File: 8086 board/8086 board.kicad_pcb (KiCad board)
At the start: 2 copper layers, 94 x 90 mm, 157 parts, among them J1 8086 bus, J2 USB, J3 RGB LCD, J4 UART, J5 AVR-ISP-6, SW33 RESET, SW34 MEM_BANK, U1 P8086-2, U10 29F800BA, U11 IS61C6416AL, U12 IS61C6416AL, U13 74AC573, U14 74AC573, U15 74AC573, U16 74AC573, U17 74LVC245A, U18 74LVC245A, U19 74LVC245A, U2 74HC32, U20 ATmega328P, U21 74HC595, U22 74HC595, U23 74HC595, U24 74HC165, U25 74HC165, U3 AMS1117-3.3, U4 CH340C, U5 74AC573, U6 74AC573, U7 74AC573, U8 74HC138, U9 74HC138, Y1 16MHz

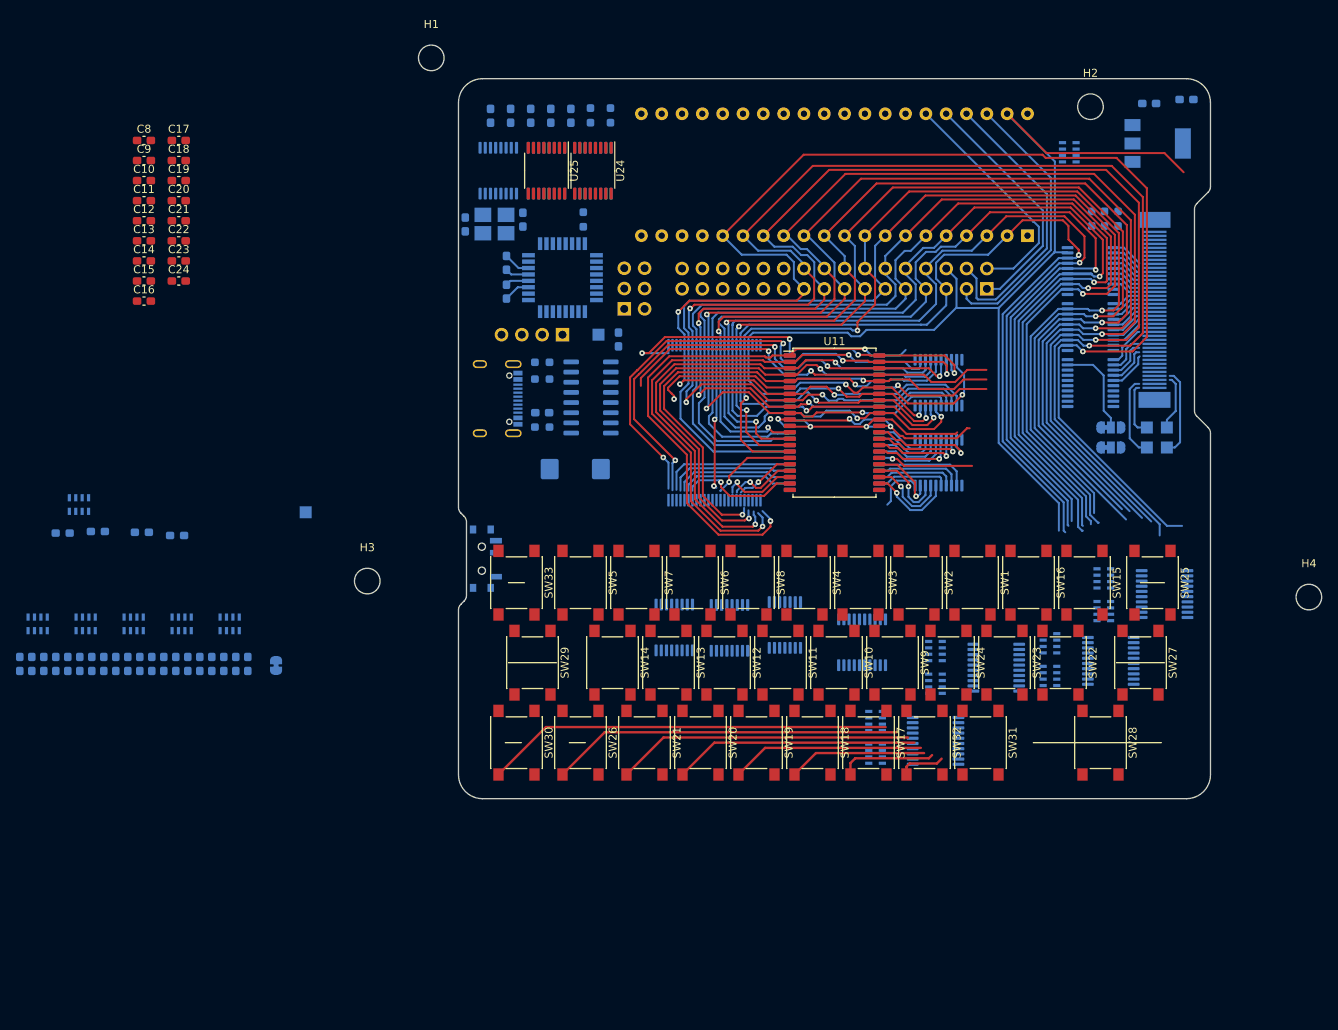
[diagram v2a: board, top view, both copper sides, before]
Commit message: PCB: layout and routing of IO, shift registers, and MCU
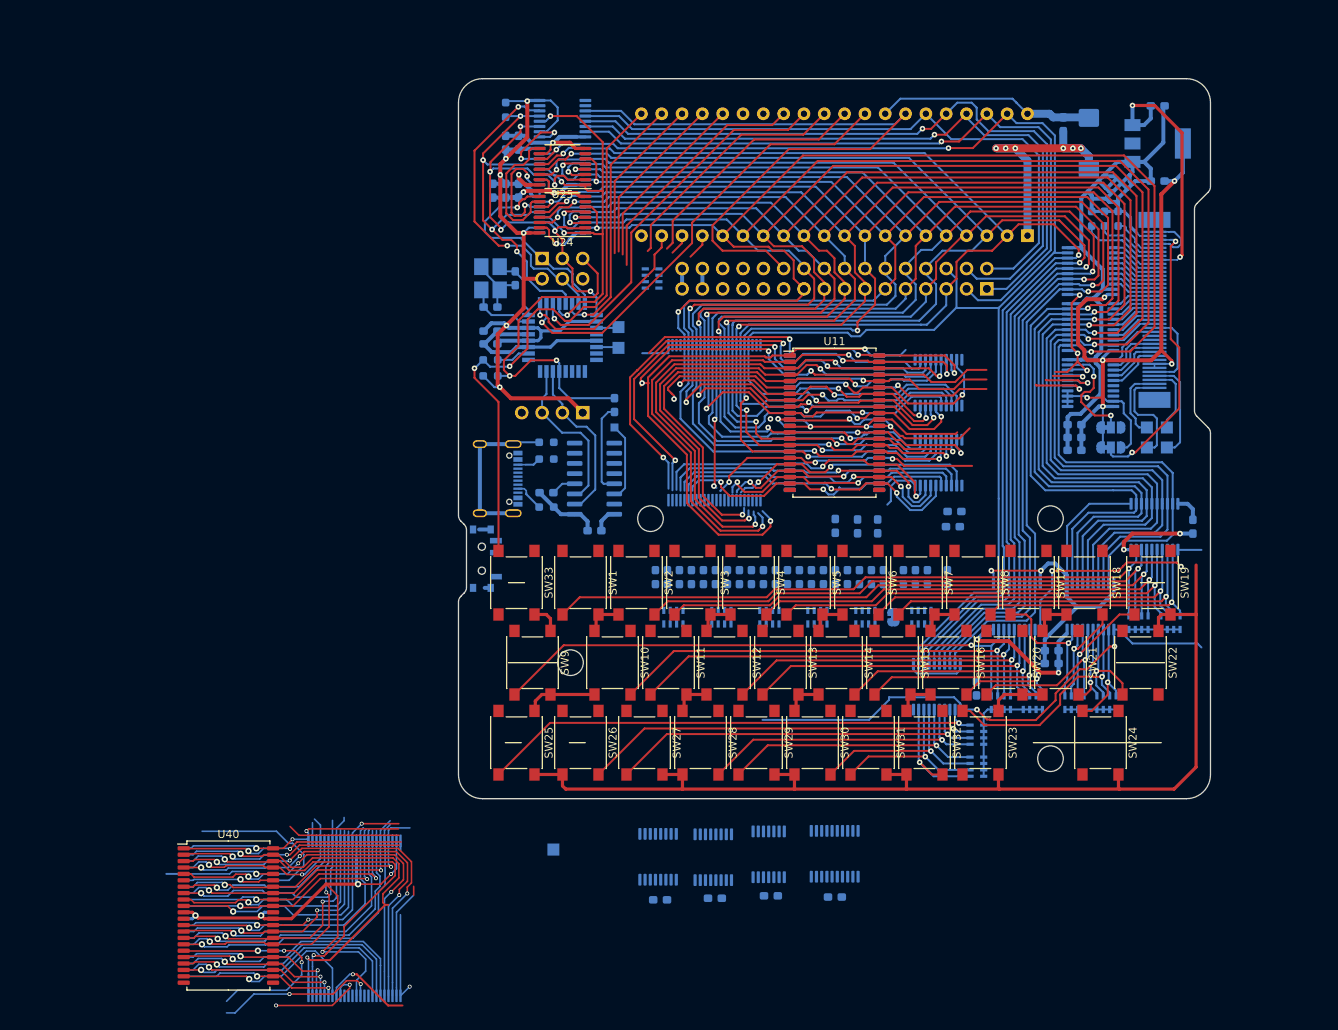
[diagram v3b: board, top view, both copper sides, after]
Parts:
- added C32: 1uF, Capacitor_SMD:C_0603_1608Metric_Pad1.08x0.95mm_HandSolder, B.Cu at (177.4, 45.1)
- added TP7: ADC6, TestPoint:TestPoint_Pad_1.5x1.5mm, B.Cu at (121.8, 70.4)
- added TP8: ADC7, TestPoint:TestPoint_Pad_1.5x1.5mm, B.Cu at (121.8, 73.0)
- added U39: 29F800BA, Package_SO:TSOP-I-48_18.4x12mm_P0.5mm, B.Cu at (88.8, 144.3)
- added U40: IS61C6416AL, Package_SO:TSOP-II-44_10.16x18.41mm_P0.8mm, F.Cu at (73.0, 144.0)
- C10, C11, C12, C13, C14, C15, C16, C17, C18, C19, C20, C21, C22, C23, C24, C8, C9: moved to B.Cu
- H1, H2, H3, H4: footprint MountingHole:MountingHole_3.2mm_M3 -> MountingHole:MountingHole_3.2mm_M3_DIN965; moved to B.Cu
- TP1: footprint TestPoint:TestPoint_Pad_1.5x1.5mm -> TestPoint:TestPoint_Pad_1.0x1.0mm
- moved C21 132.4 mm to (193.6, 95.4), turned to -90 degrees
- moved C20 123.5 mm to (175.9, 112.5)
- moved C22 120.5 mm to (175.9, 110.9)
- moved C17 117.5 mm to (178.8, 82.6), turned to 180 degrees
- moved C14 117.4 mm to (148.8, 141.7), turned to 180 degrees
- moved C18 117.2 mm to (178.8, 84.2), turned to 180 degrees
- moved C19 116.9 mm to (178.8, 85.8), turned to 180 degrees
- moved C23 113.1 mm to (166.5, 115.6), turned to -90 degrees
- moved C15 109.8 mm to (140.8, 141.5), turned to 180 degrees
- moved C11 109.0 mm to (163.6, 95.4), turned to 180 degrees
- moved D20 108.5 mm to (154.9, 101.7)
- moved C12 107.6 mm to (163.8, 93.5)
- moved RA7 106.2 mm to (159.6, 106.7)
- moved D19 105.5 mm to (153.4, 101.7)
- moved D23 105.2 mm to (157.4, 101.7), turned to 90 degrees
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- renumbered SW5 to SW1, SW14 to SW10, SW13 to SW11, SW11 to SW13, SW10 to SW14, SW9 to SW15, SW24 to SW16, SW16 to SW17, SW15 to SW18, SW25 to SW19, SW7 to SW2, SW23 to SW20, SW22 to SW21, SW27 to SW22, SW31 to SW23, SW28 to SW24, SW30 to SW25, SW21 to SW27, SW20 to SW28, SW19 to SW29, SW6 to SW3, SW18 to SW30, SW17 to SW31, SW8 to SW4, SW4 to SW5, SW3 to SW6, SW2 to SW7, SW1 to SW8, SW29 to SW9
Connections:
- net /Microcontroller/REG_OE renamed /Microcontroller/REG_~{OE}
- C17 pad 1: +5V -> +3.3V
- C18 pad 1: +5V -> +3.3V
- C19 pad 1: +5V -> +3.3V
- D1 pad 1: Net-(D1-A) -> /Memory/LA0
- D1 pad 2: /Memory/LED_CC -> Net-(D1-K)
- D10 pad 1: Net-(D10-A) -> /Memory/LA9
- D10 pad 2: /Memory/LED_CC -> Net-(D10-K)
- D11 pad 1: Net-(D11-A) -> /Memory/LA10
- D11 pad 2: /Memory/LED_CC -> Net-(D11-K)
- D12 pad 1: Net-(D12-A) -> /Memory/LA11
- D12 pad 2: /Memory/LED_CC -> Net-(D12-K)
- D13 pad 1: Net-(D13-A) -> /Memory/LA12
- D13 pad 2: /Memory/LED_CC -> Net-(D13-K)
- D14 pad 1: Net-(D14-A) -> /Memory/LA13
- D14 pad 2: /Memory/LED_CC -> Net-(D14-K)
- D15 pad 1: Net-(D15-A) -> /Memory/LA14
- D15 pad 2: /Memory/LED_CC -> Net-(D15-K)
- D16 pad 1: Net-(D16-A) -> /Memory/LA15
- D16 pad 2: /Memory/LED_CC -> Net-(D16-K)
- D17 pad 1: Net-(D17-A) -> /IO/D/~{C}
- D17 pad 2: /Memory/LED_CC -> Net-(D17-K)
- D18 pad 1: Net-(D18-A) -> /Memory/LA17
- D18 pad 2: /Memory/LED_CC -> Net-(D18-K)
- D19 pad 1: Net-(D19-A) -> /Memory/LA18
- D19 pad 2: /Memory/LED_CC -> Net-(D19-K)
- D2 pad 1: Net-(D2-A) -> /Memory/LA1
- D2 pad 2: /Memory/LED_CC -> Net-(D2-K)
- D20 pad 1: Net-(D20-A) -> /Memory/LA19
- D20 pad 2: /Memory/LED_CC -> Net-(D20-K)
- D3 pad 1: Net-(D3-A) -> /Memory/LA2
- D3 pad 2: /Memory/LED_CC -> Net-(D3-K)
- D4 pad 1: Net-(D4-A) -> /Memory/LA3
- D4 pad 2: /Memory/LED_CC -> Net-(D4-K)
- D5 pad 1: Net-(D5-A) -> /Memory/LA4
- D5 pad 2: /Memory/LED_CC -> Net-(D5-K)
- D6 pad 1: Net-(D6-A) -> /Memory/LA5
- D6 pad 2: /Memory/LED_CC -> Net-(D6-K)
- D7 pad 1: Net-(D7-A) -> /Memory/LA6
- D7 pad 2: /Memory/LED_CC -> Net-(D7-K)
- D8 pad 1: Net-(D8-A) -> /Memory/LA7
- D8 pad 2: /Memory/LED_CC -> Net-(D8-K)
- D9 pad 1: Net-(D9-A) -> /Memory/LA8
- D9 pad 2: /Memory/LED_CC -> Net-(D9-K)
- RA1 pad 1: +5V -> ~{RD}
- RA1 pad 2: +5V -> ~{WR}
- RA1 pad 3: +5V -> READY
- RA1 pad 4: GND -> RESET
- RA1 pad 5: RESET -> GND
- RA1 pad 6: ~{RD} -> +5V
- RA1 pad 7: ~{WR} -> +5V
- RA1 pad 8: READY -> +5V
- RA10 pad 1: /IO/I8 -> /IO/I9
- RA10 pad 2: /IO/I9 -> /IO/I10
- RA10 pad 3: /IO/I10 -> /IO/I11
- RA10 pad 4: /IO/I11 -> /IO/I12
- RA11 pad 1: /IO/I12 -> /IO/I13
- RA11 pad 2: /IO/I13 -> /IO/I14
- RA11 pad 3: /IO/I14 -> /IO/I15
- RA11 pad 4: /IO/I15 -> /IO/I16
- RA12 pad 1: /IO/I16 -> /IO/I17
- RA12 pad 2: /IO/I17 -> /IO/I18
- RA12 pad 3: /IO/I18 -> /IO/I19
- RA12 pad 4: /IO/I19 -> /IO/I20
- RA13 pad 1: /IO/I20 -> /IO/I21
- RA13 pad 2: /IO/I21 -> /IO/I22
- RA13 pad 3: /IO/I22 -> /IO/I23
- RA13 pad 4: /IO/I23 -> /IO/I24
- RA14 pad 1: /IO/I24 -> /IO/I28
- RA14 pad 2: /IO/I25 -> /IO/I27
- RA14 pad 4: /IO/I27 -> /IO/I25
- RA15 pad 1: /IO/I28 -> /IO/I32
- RA15 pad 2: /IO/I29 -> /IO/I31
- RA15 pad 4: /IO/I31 -> /IO/I29
- RA2 pad 1: Net-(D4-A) -> /Memory/LED_CC
- RA2 pad 2: Net-(D3-A) -> /Memory/LED_CC
- RA2 pad 3: Net-(D2-A) -> /Memory/LED_CC
- RA2 pad 4: Net-(D1-A) -> /Memory/LED_CC
- RA2 pad 5: /Memory/LA0 -> Net-(D1-K)
- RA2 pad 6: /Memory/LA1 -> Net-(D2-K)
- RA2 pad 7: /Memory/LA2 -> Net-(D3-K)
- RA2 pad 8: /Memory/LA3 -> Net-(D4-K)
- RA3 pad 1: Net-(D8-A) -> /Memory/LED_CC
- RA3 pad 2: Net-(D7-A) -> /Memory/LED_CC
- RA3 pad 3: Net-(D6-A) -> /Memory/LED_CC
- RA3 pad 4: Net-(D5-A) -> /Memory/LED_CC
- RA3 pad 5: /Memory/LA4 -> Net-(D5-K)
- RA3 pad 6: /Memory/LA5 -> Net-(D6-K)
- RA3 pad 7: /Memory/LA6 -> Net-(D7-K)
- RA3 pad 8: /Memory/LA7 -> Net-(D8-K)
- RA4 pad 1: Net-(D12-A) -> /Memory/LED_CC
- RA4 pad 2: Net-(D11-A) -> /Memory/LED_CC
- RA4 pad 3: Net-(D10-A) -> /Memory/LED_CC
- RA4 pad 4: Net-(D9-A) -> /Memory/LED_CC
- RA4 pad 5: /Memory/LA8 -> Net-(D9-K)
- RA4 pad 6: /Memory/LA9 -> Net-(D10-K)
- RA4 pad 7: /Memory/LA10 -> Net-(D11-K)
- RA4 pad 8: /Memory/LA11 -> Net-(D12-K)
- RA5 pad 1: Net-(D16-A) -> /Memory/LED_CC
- RA5 pad 2: Net-(D15-A) -> /Memory/LED_CC
- RA5 pad 3: Net-(D14-A) -> /Memory/LED_CC
- RA5 pad 4: Net-(D13-A) -> /Memory/LED_CC
- RA5 pad 5: /Memory/LA12 -> Net-(D13-K)
- RA5 pad 6: /Memory/LA13 -> Net-(D14-K)
- RA5 pad 7: /Memory/LA14 -> Net-(D15-K)
- RA5 pad 8: /Memory/LA15 -> Net-(D16-K)
- RA6 pad 1: Net-(D20-A) -> /Memory/LED_CC
- RA6 pad 2: Net-(D19-A) -> /Memory/LED_CC
- RA6 pad 3: Net-(D18-A) -> /Memory/LED_CC
- RA6 pad 4: Net-(D17-A) -> /Memory/LED_CC
- RA6 pad 5: /IO/D/~{C} -> Net-(D17-K)
- RA6 pad 6: /Memory/LA17 -> Net-(D18-K)
- RA6 pad 7: /Memory/LA18 -> Net-(D19-K)
- RA6 pad 8: /Memory/LA19 -> Net-(D20-K)
- RA7 pad 1: Net-(D24-A) -> +5V
- RA7 pad 2: Net-(D23-A) -> +5V
- RA7 pad 3: Net-(D22-A) -> +5V
- RA7 pad 4: Net-(D21-A) -> +5V
- RA7 pad 5: +5V -> Net-(D23-A)
- RA7 pad 6: +5V -> Net-(D22-A)
- RA7 pad 7: +5V -> Net-(D21-A)
- RA7 pad 8: +5V -> Net-(D24-A)
- RA8 pad 1: /IO/I0 -> GND
- RA8 pad 2: /IO/I1 -> GND
- RA8 pad 3: /IO/I2 -> GND
- RA8 pad 4: /IO/I3 -> GND
- RA8 pad 5: GND -> /IO/I1
- RA8 pad 6: GND -> /IO/I2
- RA8 pad 7: GND -> /IO/I3
- RA8 pad 8: GND -> /IO/I4
- RA9 pad 1: /IO/I4 -> GND
- RA9 pad 2: /IO/I5 -> GND
- RA9 pad 3: /IO/I6 -> GND
- RA9 pad 4: /IO/I7 -> GND
- RA9 pad 5: GND -> /IO/I5
- RA9 pad 6: GND -> /IO/I6
- RA9 pad 7: GND -> /IO/I7
- RA9 pad 8: GND -> /IO/I8
- SW1 pad 2: /IO/I4 -> /IO/I1
- SW10 pad 1: +5V -> /IO/I10
- SW10 pad 2: /IO/I13 -> +5V
- SW11 pad 2: /IO/I12 -> /IO/I11
- SW12 pad 1: +5V -> /IO/I12
- SW12 pad 2: /IO/I11 -> +5V
- SW13 pad 2: /IO/I10 -> /IO/I13
- SW14 pad 1: +5V -> /IO/I14
- SW14 pad 2: /IO/I9 -> +5V
- SW15 pad 2: /IO/I8 -> /IO/I15
- SW16 pad 1: +5V -> /IO/I16
- SW16 pad 2: /IO/I23 -> +5V
- SW17 pad 2: /IO/I15 -> /IO/I17
- SW18 pad 1: +5V -> /IO/I18
- SW18 pad 2: /IO/I14 -> +5V
- SW19 pad 2: /IO/I24 -> /IO/I19
- SW2 pad 1: +5V -> /IO/I2
- SW2 pad 2: /IO/I6 -> +5V
- SW20 pad 2: /IO/I22 -> /IO/I20
- SW21 pad 1: +5V -> /IO/I21
- SW21 pad 2: /IO/I21 -> +5V
- SW22 pad 2: /IO/I26 -> /IO/I22
- SW23 pad 2: /IO/I30 -> /IO/I23
- SW24 pad 2: /IO/I27 -> /IO/I24
- SW25 pad 2: /IO/I29 -> /IO/I25
- SW26 pad 1: +5V -> /IO/I26
- SW26 pad 2: /IO/I25 -> +5V
- SW27 pad 2: /IO/I20 -> /IO/I27
- SW28 pad 1: +5V -> /IO/I28
- SW28 pad 2: /IO/I19 -> +5V
- SW29 pad 2: /IO/I18 -> /IO/I29
- SW3 pad 2: /IO/I5 -> /IO/I3
- SW30 pad 1: +5V -> /IO/I30
- SW30 pad 2: /IO/I17 -> +5V
- SW31 pad 2: /IO/I16 -> /IO/I31
- SW32 pad 1: +5V -> /IO/I32
- SW32 pad 2: /IO/I31 -> +5V
- SW4 pad 1: +5V -> /IO/I4
- SW4 pad 2: /IO/I7 -> +5V
- SW5 pad 2: /IO/I3 -> /IO/I5
- SW6 pad 1: +5V -> /IO/I6
- SW6 pad 2: /IO/I2 -> +5V
- SW7 pad 2: /IO/I1 -> /IO/I7
- SW8 pad 1: +5V -> /IO/I8
- SW8 pad 2: /IO/I0 -> +5V
- SW9 pad 2: /IO/I28 -> /IO/I9
- U13 pad 12: AD0 -> AD7
- U13 pad 13: AD1 -> AD6
- U13 pad 14: AD2 -> AD5
- U13 pad 15: AD3 -> AD4
- U13 pad 16: AD4 -> AD3
- U13 pad 17: AD5 -> AD2
- U13 pad 18: AD6 -> AD1
- U13 pad 19: AD7 -> AD0
- U13 pad 2: /IO/I7 -> /IO/I8
- U13 pad 3: /IO/I6 -> /IO/I7
- U13 pad 4: /IO/I5 -> /IO/I6
- U13 pad 5: /IO/I4 -> /IO/I5
- U13 pad 6: /IO/I3 -> /IO/I4
- U13 pad 7: /IO/I2 -> /IO/I3
- U13 pad 8: /IO/I1 -> /IO/I2
- U13 pad 9: /IO/I0 -> /IO/I1
- U14 pad 2: /IO/I8 -> /IO/I16
- U14 pad 3: /IO/I9 -> /IO/I15
- U14 pad 4: /IO/I10 -> /IO/I14
- U14 pad 5: /IO/I11 -> /IO/I13
- U14 pad 7: /IO/I13 -> /IO/I11
- U14 pad 8: /IO/I14 -> /IO/I10
- U14 pad 9: /IO/I15 -> /IO/I9
- U15 pad 12: AD0 -> AD7
- U15 pad 13: AD1 -> AD6
- U15 pad 14: AD2 -> AD5
- U15 pad 15: AD3 -> AD4
- U15 pad 16: AD4 -> AD3
- U15 pad 17: AD5 -> AD2
- U15 pad 18: AD6 -> AD1
- U15 pad 19: AD7 -> AD0
- U15 pad 2: /IO/I23 -> /IO/I24
- U15 pad 3: /IO/I22 -> /IO/I23
- U15 pad 4: /IO/I21 -> /IO/I22
- U15 pad 5: /IO/I20 -> /IO/I21
- U15 pad 6: /IO/I19 -> /IO/I20
- U15 pad 7: /IO/I18 -> /IO/I19
- U15 pad 8: /IO/I17 -> /IO/I18
- U15 pad 9: /IO/I16 -> /IO/I17
- U16 pad 2: /IO/I24 -> /IO/I25
- U16 pad 3: /IO/I25 -> /IO/I26
- U16 pad 4: /IO/I26 -> /IO/I27
- U16 pad 5: /IO/I27 -> /IO/I28
- U16 pad 6: /IO/I28 -> /IO/I29
- U16 pad 7: /IO/I29 -> /IO/I30
- U16 pad 8: /IO/I30 -> /IO/I31
- U16 pad 9: /IO/I31 -> /IO/I32
- U19 pad 2: unconnected-(U19-A0-Pad2) -> +3.3V
- U19 pad 3: unconnected-(U19-A1-Pad3) -> +3.3V
- U19 pad 4: unconnected-(U19-A2-Pad4) -> +3.3V
- U20 pad 19: unconnected-(U20-ADC6-Pad19) -> Net-(U20-ADC6)
- U20 pad 22: unconnected-(U20-ADC7-Pad22) -> Net-(U20-ADC7)
- U21 pad 1: AD1 -> AD6
- U21 pad 14: /Microcontroller/SPI_MOSI -> Net-(U21-SER)
- U21 pad 15: AD0 -> AD7
- U21 pad 2: AD2 -> AD5
- U21 pad 3: AD3 -> AD4
- U21 pad 4: AD4 -> AD3
- U21 pad 5: AD5 -> AD2
- U21 pad 6: AD6 -> AD1
- U21 pad 7: AD7 -> AD0
- U21 pad 9: Net-(U21-QH') -> unconnected-(U21-QH'-Pad9)
- U22 pad 1: AD9 -> AD14
- U22 pad 14: Net-(U21-QH') -> Net-(U22-SER)
- U22 pad 15: AD8 -> AD15
- U22 pad 2: AD10 -> AD13
- U22 pad 3: AD11 -> AD12
- U22 pad 4: AD12 -> AD11
- U22 pad 5: AD13 -> AD10
- U22 pad 6: AD14 -> AD9
- U22 pad 7: AD15 -> AD8
- U22 pad 9: Net-(U22-QH') -> Net-(U21-SER)
- U23 pad 1: A17 -> unconnected-(U23-QB-Pad1)
- U23 pad 14: Net-(U22-QH') -> /Microcontroller/SPI_MOSI
- U23 pad 15: A16 -> unconnected-(U23-QA-Pad15)
- U23 pad 2: A18 -> unconnected-(U23-QC-Pad2)
- U23 pad 3: A19 -> ~{BHE}
- U23 pad 4: unconnected-(U23-QE-Pad4) -> A19
- U23 pad 5: unconnected-(U23-QF-Pad5) -> A18
- U23 pad 6: unconnected-(U23-QG-Pad6) -> A17
- U23 pad 7: ~{BHE} -> A16
- U23 pad 9: unconnected-(U23-QH'-Pad9) -> Net-(U22-SER)
- U24 pad 10: GND -> Net-(U24-SER)
- U24 pad 11: AD0 -> AD7
- U24 pad 12: AD1 -> AD6
- U24 pad 13: AD2 -> AD5
- U24 pad 14: AD3 -> AD4
- U24 pad 3: AD4 -> AD3
- U24 pad 4: AD5 -> AD2
- U24 pad 5: AD6 -> AD1
- U24 pad 6: AD7 -> AD0
- U24 pad 9: Net-(U24-QH) -> /Microcontroller/SPI_MISO
- U25 pad 10: Net-(U24-QH) -> GND
- U25 pad 11: AD8 -> AD15
- U25 pad 12: AD9 -> AD14
- U25 pad 13: AD10 -> AD13
- U25 pad 14: AD11 -> AD12
- U25 pad 3: AD12 -> AD11
- U25 pad 4: AD13 -> AD10
- U25 pad 5: AD14 -> AD9
- U25 pad 6: AD15 -> AD8
- U25 pad 9: /Microcontroller/SPI_MISO -> Net-(U24-SER)
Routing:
- net +5V: track 60.1 -> 557.3 mm, vias 5 -> 21
- net GND: track 33.1 -> 340.3 mm, vias 2 -> 16
- net AD7: track 141.0 -> 260.6 mm, vias 3 -> 6
- net AD9: track 151.3 -> 267.0 mm, vias 2 -> 6
- net AD11: track 152.1 -> 267.2 mm, vias 3 -> 8
- net AD14: track 135.2 -> 247.8 mm, vias 3 -> 6
- net AD13: track 140.2 -> 252.6 mm, vias 3 -> 6
- net AD6: track 144.7 -> 255.8 mm, vias 3 -> 6
- net AD5: track 147.9 -> 257.3 mm, vias 3 -> 6
- net AD10: track 148.8 -> 257.9 mm, vias 2 -> 6
- net AD8: track 155.5 -> 263.0 mm, vias 2 -> 6
- net AD4: track 153.4 -> 260.2 mm, vias 3 -> 6
- net AD12: track 150.4 -> 256.0 mm, vias 3 -> 6
- net ~{RD}: track 49.0 -> 149.1 mm, vias 2 -> 8
- net AD15: track 156.8 -> 251.6 mm, vias 2 -> 6
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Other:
- outline, holes or cut-outs redrawn
- board text added: "MEM"
- board text removed: "hold reset button while programming!"

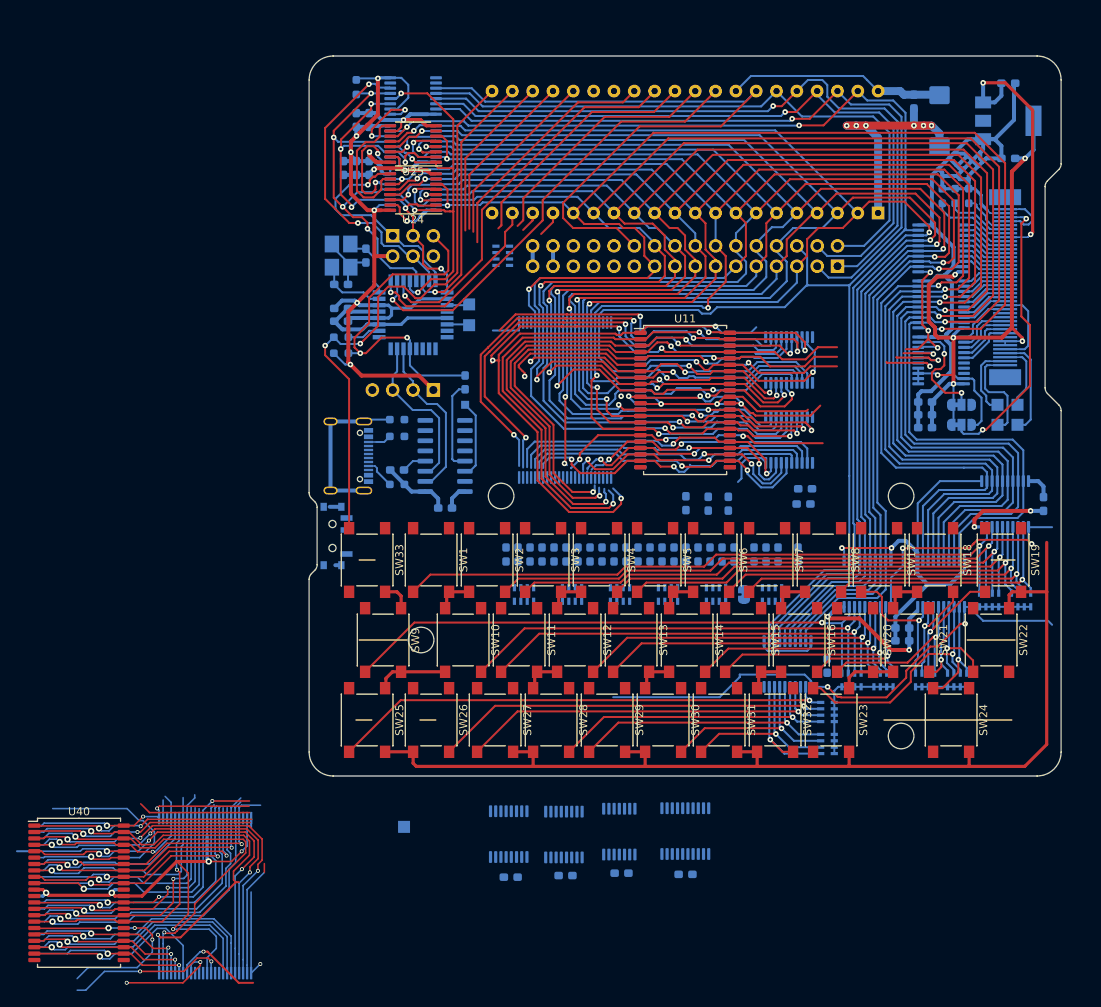
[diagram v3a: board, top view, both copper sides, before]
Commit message: finish routing PCB
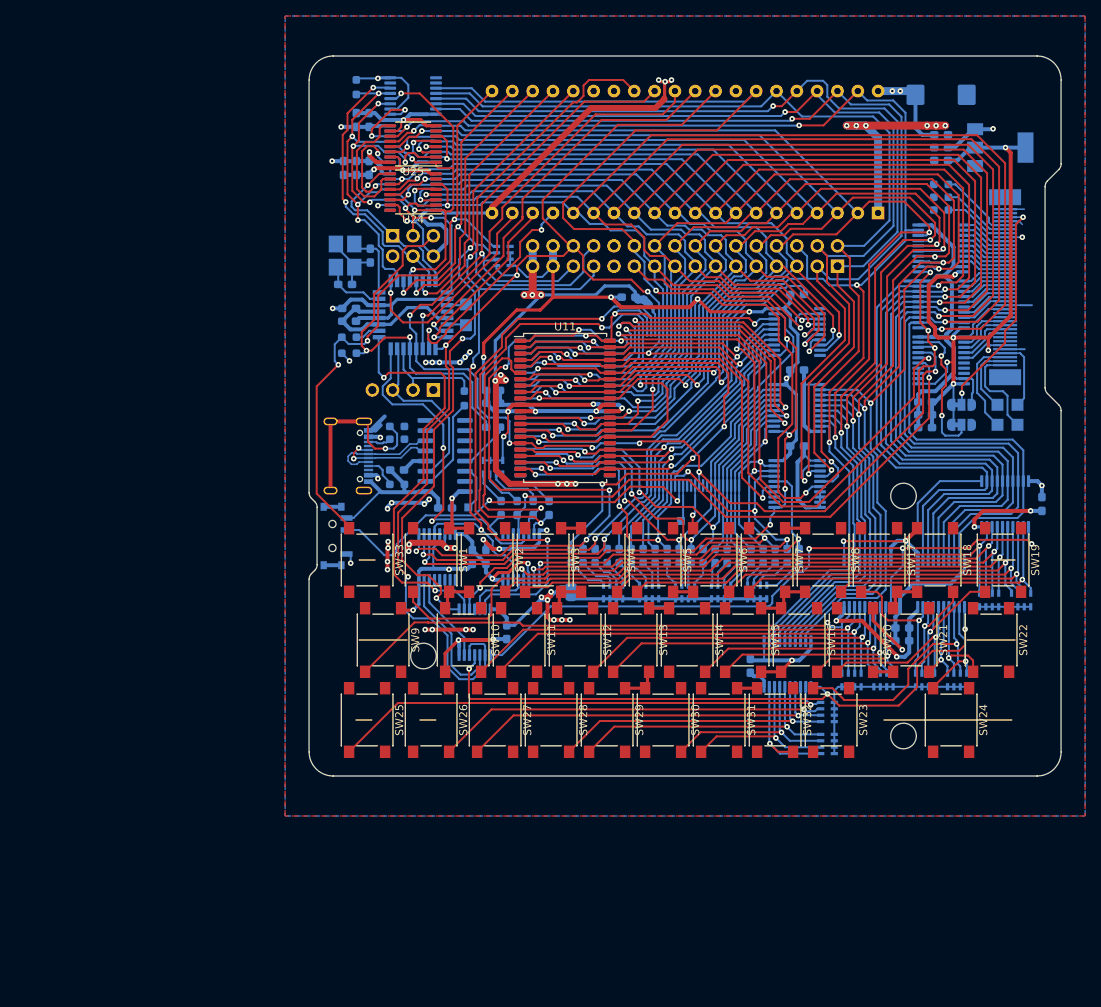
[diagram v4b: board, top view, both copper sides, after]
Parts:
- removed the H1 at (125.8, 94.4)
- removed U39: 29F800BA, Package_SO:TSOP-I-48_18.4x12mm_P0.5mm
- removed U40: IS61C6416AL, Package_SO:TSOP-II-44_10.16x18.41mm_P0.8mm
- added R10: 1k, Resistor_SMD:R_0603_1608Metric_Pad0.98x0.95mm_HandSolder, B.Cu at (121.2, 82.2)
- D21: value FLASH -> MCU
- D22: value RAM1 -> LCD
- D24: value POWER -> RAM1
- RA10, RA11, RA12, RA13, RA14, RA15, RA8, RA9: value 220R -> 10k
- RA2, RA3, RA4, RA5, RA6, RA7: value 220R -> 1k
- SW1: value ~ -> Q
- SW10: value ~ -> A
- SW11: value ~ -> S
- SW12: value ~ -> D
- SW13: value ~ -> F
- SW14: value ~ -> G
- SW15: value ~ -> H
- SW16: value ~ -> J
- SW17: value ~ -> O
- SW18: value ~ -> P
- SW19: value ~ -> Backspace
- SW2: value ~ -> W
- SW20: value ~ -> K
- SW21: value ~ -> L
- SW22: value ~ -> enter
- SW23: value ~ -> M
- SW24: value ~ -> space
- SW25: value ~ -> alt
- SW26: value ~ -> ctrl
- SW27: value ~ -> Z
- SW28: value ~ -> X
- SW29: value ~ -> C
- SW3: value ~ -> E
- SW30: value ~ -> V
- SW31: value ~ -> B
- SW32: value ~ -> N
- SW34: footprint Button_Switch_SMD:SW_SPDT_PCM12 -> 8086PC:SW_SPDT_PCM12
- SW4: value ~ -> R
- SW5: value ~ -> T
- SW6: value ~ -> Y
- SW7: value ~ -> U
- SW8: value ~ -> I
- SW9: value ~ -> shift
- TP2: footprint TestPoint:TestPoint_Pad_1.5x1.5mm -> TestPoint:TestPoint_Pad_1.0x1.0mm
- moved C14 72.5 mm to (141.7, 69.5), turned to 0 degrees
- moved TP2 51.6 mm to (148.2, 97.5), turned to 180 degrees
- moved U7 45.6 mm to (162.8, 92.9), turned to 180 degrees
- moved C24 41.0 mm to (123.9, 102.0), turned to -90 degrees
- moved C12 40.9 mm to (124.8, 81.2)
- moved C11 40.8 mm to (124.8, 82.8), turned to 0 degrees
- moved C16 40.3 mm to (122.2, 102.0), turned to 90 degrees
- moved RA7 38.3 mm to (124.8, 90.8), turned to -90 degrees
- moved U9 38.1 mm to (117.8, 102.0)
- moved D21 35.1 mm to (125.8, 95.9), turned to -90 degrees
- moved U8 34.7 mm to (128.3, 102.0)
- moved C15 33.4 mm to (126.5, 111.4), turned to 90 degrees
- moved D22 31.7 mm to (127.8, 95.9), turned to -90 degrees
- moved D24 31.7 mm to (131.8, 95.9), turned to -90 degrees
- moved U2 30.8 mm to (122.5, 111.4)
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- renumbered H4 to H1
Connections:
- D21 pad 2: /Memory/~{FLASH} -> ~{MCU}
- D22 pad 2: /Memory/~{RAM1} -> ~{LCD}
- D24 pad 2: GND -> /Memory/~{RAM1}
- J1 pad 10: AD11 -> AD13
- J1 pad 11: AD8 -> AD4
- J1 pad 12: AD9 -> AD12
- J1 pad 13: AD6 -> AD3
- J1 pad 14: AD7 -> AD11
- J1 pad 15: AD4 -> AD2
- J1 pad 16: AD5 -> AD10
- J1 pad 17: AD2 -> AD1
- J1 pad 18: AD3 -> AD9
- J1 pad 20: AD1 -> AD8
- J1 pad 21: BUSALE -> ALE
- J1 pad 23: M\~{IO} -> unconnected-(J1-Pin_23-Pad23)
- J1 pad 24: READY -> unconnected-(J1-Pin_24-Pad24)
- J1 pad 25: HLDA -> M\~{IO}
- J1 pad 26: ~{WR} -> READY
- J1 pad 27: ~{RD} -> ~{WR}
- J1 pad 28: HOLD -> ~{RD}
- J1 pad 5: AD14 -> AD7
- J1 pad 7: AD12 -> AD6
- J1 pad 8: AD13 -> AD14
- J1 pad 9: AD10 -> AD5
- RA7 pad 5: Net-(D23-A) -> Net-(D24-A)
- RA7 pad 6: Net-(D22-A) -> Net-(D23-A)
- RA7 pad 7: Net-(D21-A) -> Net-(D22-A)
- RA7 pad 8: Net-(D24-A) -> Net-(D21-A)
- SW34 pad 1: GND -> +5V
- SW34 pad 3: +5V -> GND
- U2 pad 10: ~{IO1} -> ~{IO0}
- U2 pad 11: /IO/~{RD0} -> /IO/~{RD1}
- U2 pad 13: ~{IO0} -> ~{IO1}
- U2 pad 8: /IO/~{RD1} -> /IO/~{RD0}
- U20 pad 10: ~{RD} -> /Microcontroller/REG_~{OE}
- U20 pad 11: ~{WR} -> READY
- U20 pad 13: /Microcontroller/REG_~{OE} -> ~{TEST}
- U20 pad 14: READY -> ~{INTA}
- U20 pad 24: HLDA -> INTR
- U20 pad 25: INTR -> ~{RD}
- U20 pad 27: ~{INTA} -> HLDA
- U20 pad 28: ~{TEST} -> ~{WR}
- U4 pad 2: /Microcontroller/TX -> Net-(U4-TXD)
- U5 pad 16: /Memory/LA3 -> /Memory/LA11
- U5 pad 17: /Memory/LA2 -> /Memory/LA10
- U5 pad 18: /Memory/LA1 -> /Memory/LA9
- U5 pad 19: /Memory/LA0 -> /Memory/LA8
- U5 pad 2: AD0 -> AD8
- U5 pad 3: AD1 -> AD9
- U5 pad 4: AD2 -> AD10
- U5 pad 5: AD3 -> AD11
- U6 pad 12: /Memory/LA11 -> /Memory/LA7
- U6 pad 13: /Memory/LA10 -> /Memory/LA6
- U6 pad 14: /Memory/LA9 -> /Memory/LA5
- U6 pad 15: /Memory/LA8 -> /Memory/LA4
- U6 pad 16: /Memory/LA7 -> /Memory/LA3
- U6 pad 17: /Memory/LA6 -> /Memory/LA2
- U6 pad 18: /Memory/LA5 -> /Memory/LA1
- U6 pad 19: /Memory/LA4 -> /Memory/LA0
- U6 pad 2: AD4 -> AD0
- U6 pad 3: AD5 -> AD1
- U6 pad 4: AD6 -> AD2
- U6 pad 5: AD7 -> AD3
- U6 pad 6: AD8 -> AD4
- U6 pad 7: AD9 -> AD5
- U6 pad 8: AD10 -> AD6
- U6 pad 9: AD11 -> AD7
- U7 pad 12: /Memory/~{LBHE} -> unconnected-(U7-O7-Pad12)
- U7 pad 13: /Memory/LA19 -> unconnected-(U7-O6-Pad13)
- U7 pad 14: /Memory/LA18 -> unconnected-(U7-O5-Pad14)
- U7 pad 15: /Memory/LA17 -> /Memory/~{LBHE}
- U7 pad 16: /IO/D/~{C} -> /Memory/LA19
- U7 pad 17: unconnected-(U7-O2-Pad17) -> /Memory/LA18
- U7 pad 18: unconnected-(U7-O1-Pad18) -> /Memory/LA17
- U7 pad 19: unconnected-(U7-O0-Pad19) -> /IO/D/~{C}
- U7 pad 2: GND -> A16
- U7 pad 3: GND -> A17
- U7 pad 4: GND -> A18
- U7 pad 5: A16 -> A19
- U7 pad 6: A17 -> ~{BHE}
- U7 pad 7: A18 -> GND
- U7 pad 8: A19 -> GND
- U7 pad 9: ~{BHE} -> GND
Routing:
- net +5V: track 557.3 -> 397.9 mm, vias 21 -> 47
- net GND: track 340.3 -> 481.9 mm, vias 16 -> 48
- net ALE: track 0.00 -> 98.2 mm, vias 0 -> 5
- net ~{RD}: track 149.1 -> 236.6 mm, vias 8 -> 9
- net M\~{IO}: track 30.3 -> 103.3 mm, vias 0 -> 3
- net /Memory/~{FLASH}: track 2.27 -> 71.8 mm, vias 0 -> 2
- net ~{LCD}: track 7.33 -> 71.4 mm, vias 1 -> 2
- net /Memory/LA17: track 1.20 -> 64.2 mm, vias 0 -> 4
- net AD11: track 267.2 -> 204.7 mm, vias 8 -> 5
- net AD9: track 267.0 -> 208.3 mm, vias 6 -> 5
- net /CPUALE: track 22.8 -> 81.3 mm, vias 0 -> 3
- net /Memory/LA19: track 0.00 -> 58.0 mm, vias 0 -> 2
- net /IO/~{RD0}: track 30.0 -> 85.9 mm, vias 2 -> 3
- net AD10: track 257.9 -> 202.4 mm, vias 6 -> 5
- net AD12: track 256.0 -> 203.8 mm, vias 6 -> 5
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- added copper zone on F.Cu, net +5V
- added copper zone on B.Cu, net GND
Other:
- board text removed: "MEM"
